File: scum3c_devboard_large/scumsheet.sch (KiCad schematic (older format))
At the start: 15 parts, among them U8 scum3

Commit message: ready for merge
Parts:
- removed C13, C14, C15, C16, C17, C18, C19, C20, C21, C22, C24: NP, Capacitor_SMD:C_0402_1005Metric, symbol Device:C
- removed R12, R13, R14: NP, Resistor_SMD:R_0402_1005Metric, symbol Device:R_US
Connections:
- net labels removed: +VDD25, +VDDAO, AUX_LDO_OUTPUT, GP4, GP5, GP6, GP7, VDDD_DISABLE, VDD_AO_DISABLE
- wire segments 24 -> 0
- no-connect marks 44 -> 52

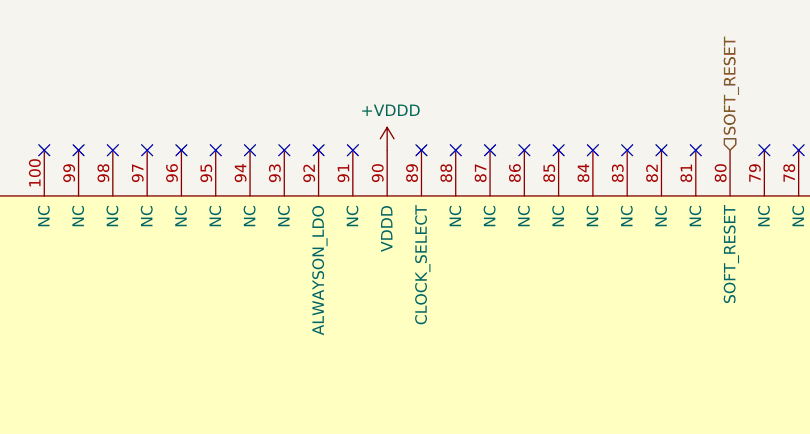
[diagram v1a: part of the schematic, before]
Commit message: replaced level shifters and other changes
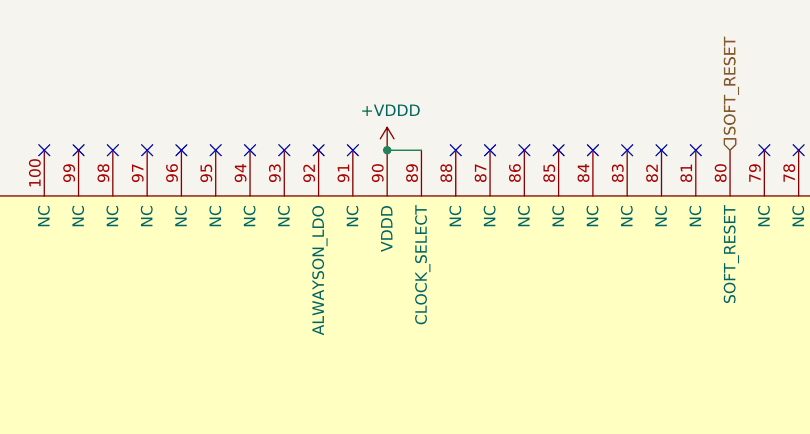
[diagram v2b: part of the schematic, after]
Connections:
- net +VDDD: now also U8.89 (CLOCK_SELECT)
- no-connect marks 52 -> 51
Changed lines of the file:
@@
 NoConn ~ 2250 3800
 NoConn ~ 2250 4550
-NoConn ~ 2250 4700
 NoConn ~ 2250 4850
 NoConn ~ 2250 5000
@@
 NoConn ~ 2250 5450
 NoConn ~ 2250 5600
-NoConn ~ 8000 1950
 NoConn ~ 8000 2100
 NoConn ~ 8000 2250
@@
 NoConn ~ 8000 2550
 NoConn ~ 8000 2700
-NoConn ~ 5000 1150
 NoConn ~ 2250 3350
 NoConn ~ 2250 5150
-NoConn ~ 8000 2400
 NoConn ~ 2250 3650
 NoConn ~ 4550 1150
+NoConn ~ 8000 2400
+Wire Wire Line
+	5000 1150 4850 1150
+Connection ~ 4850 1150
+NoConn ~ 2250 4700
+NoConn ~ 8000 1950
 $EndSCHEMATC

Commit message: Suggested changes
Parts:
- added J14, J15: Conn_01x01_Male, Connector_PinHeader_2.54mm:PinHeader_1x01_P2.54mm_Vertical, symbol Connector:Conn_01x01_Male
- U8: symbol draft1library:scum3 -> SCUM:scum3
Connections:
- net at U8.53 (SENSOR_LDO_OUTPUT): now also J15.1 (Pin_1)
- net at U8.54 (SENSOR_EXT_IN): now also J14.1 (Pin_1)
- no-connect marks 51 -> 49
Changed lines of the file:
@@
 EESchema Schematic File Version 4
 LIBS:scum3c-devboard-cache
-EELAYER 26 0
+EELAYER 30 0
 EELAYER END
 $Descr A4 11693 8268
 encoding utf-8
-Sheet 2 4
+Sheet 4 4
 Title ""
 Date ""
@@
 $EndDescr
 $Comp
-L draft1library:scum3 U8
+L SCUM:scum3 U8
 U 1 1 5F3B2246
 P 5200 3450
@@
 NoConn ~ 8000 5550
 NoConn ~ 8000 5400
-NoConn ~ 8000 5250
-NoConn ~ 8000 5100
 NoConn ~ 6950 1150
 NoConn ~ 6800 1150
@@
 $EndComp
 $Comp
-L draft1library:+VBAT #PWR0170
+L SCUM:+VBAT #PWR0170
 U 1 1 5F3D3274
 P 2250 2450
@@
 $EndComp
 $Comp
-L draft1library:+VBAT #PWR0176
+L SCUM:+VBAT #PWR0176
 U 1 1 5F3DA21E
 P 2250 4400
@@
 $EndComp
 $Comp
-L draft1library:+VBAT #PWR0193
+L SCUM:+VBAT #PWR0193
 U 1 1 5F40149D
 P 3100 6050
@@
 GPIO15
 $Comp
-L draft1library:+VDDIO #PWR0194
+L SCUM:+VDDIO #PWR0194
 U 1 1 5F404D67
 P 4900 6050
@@
 HARD_RESET
 $Comp
-L draft1library:+VBAT #PWR0195
+L SCUM:+VBAT #PWR0195
 U 1 1 5F406DAE
 P 8000 4350
@@
 ASC_PHI2
 $Comp
-L draft1library:+VBAT #PWR0196
+L SCUM:+VBAT #PWR0196
 U 1 1 5F407E52
 P 8000 3900
@@
 ASC_EXT_OVERRIDE
 $Comp
-L draft1library:+VDDD #PWR0207
+L SCUM:+VDDD #PWR0207
 U 1 1 5F3A7150
 P 4850 1150
@@
 Wire Wire Line
 	5000 1150 4850 1150
-Connection ~ 4850 1150
 NoConn ~ 2250 4700
 NoConn ~ 8000 1950
+$Comp
+L Connector:Conn_01x01_Male J14
+U 1 1 607AD522
+P 8200 5100
+F 0 "J14" H 8172 5032 50  0000 R CNN
+F 1 "Conn_01x01_Male" H 8172 5123 50  0000 R CNN
+F 2 "Connector_PinHeader_2.54mm:PinHeader_1x01_P2.54mm_Vertical" H 8200 5100 50  0001 C CNN
+F 3 "~" H 8200 5100 50  0001 C CNN
+	1    8200 5100
+	-1   0    0    1
+$EndComp
+$Comp
+L Connector:Conn_01x01_Male J15
+U 1 1 607AEA7E
+P 8200 5250
+F 0 "J15" H 8172 5182 50  0000 R CNN
+F 1 "Conn_01x01_Male" H 8172 5273 50  0000 R CNN
+F 2 "Connector_PinHeader_2.54mm:PinHeader_1x01_P2.54mm_Vertical" H 8200 5250 50  0001 C CNN
+F 3 "~" H 8200 5250 50  0001 C CNN
+	1    8200 5250
+	-1   0    0    1
+$EndComp
 $EndSCHEMATC

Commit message: switching computers
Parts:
- removed J14, J15: Conn_01x01_Male, Connector_PinHeader_2.54mm:PinHeader_1x01_P2.54mm_Vertical, symbol Connector:Conn_01x01_Male
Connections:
- net ADC_LDO_OUT: now reaches U8.53 (SENSOR_LDO_OUTPUT)
- net ADC_IN: now reaches U8.54 (SENSOR_EXT_IN)
- net GPO_ZERO: now reaches U8.57 (GPO_ZERO)
- net +VBAT renamed +VBATSCuM
- net +VDDIO renamed +VDDIOSCuM
- net SOFT_RESET: no longer names the net of U8.80 (SOFT_RESET)
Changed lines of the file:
@@
 NoConn ~ 8000 2100
 NoConn ~ 8000 2250
-NoConn ~ 8000 4650
 NoConn ~ 8000 5550
 NoConn ~ 8000 5400
@@
 $EndComp
 $Comp
-L SCUM:+VBAT #PWR0170
-U 1 1 5F3D3274
-P 2250 2450
-AR Path="/5F3B1D81/5F3D3274" Ref="#PWR0170"  Part="1"
-AR Path="/5F41418C/5F3D3274" Ref="#PWR?"  Part="1"
-AR Path="/5F414989/5F3D3274" Ref="#PWR?"  Part="1"
-F 0 "#PWR0170" H 2250 2300 50  0001 C CNN
-F 1 "+VBAT" V 2265 2578 50  0000 L CNN
-F 2 "" H 2250 2450 50  0001 C CNN
-F 3 "" H 2250 2450 50  0001 C CNN
-	1    2250 2450
-	0    -1   -1   0
-$EndComp
-$Comp
 L power:GND #PWR0171
 U 1 1 5F3D443B
@@
 	1    2250 4250
 	0    1    1    0
-$EndComp
-$Comp
-L SCUM:+VBAT #PWR0176
-U 1 1 5F3DA21E
-P 2250 4400
-AR Path="/5F3B1D81/5F3DA21E" Ref="#PWR0176"  Part="1"
-AR Path="/5F41418C/5F3DA21E" Ref="#PWR?"  Part="1"
-AR Path="/5F414989/5F3DA21E" Ref="#PWR?"  Part="1"
-F 0 "#PWR0176" H 2250 4250 50  0001 C CNN
-F 1 "+VBAT" V 2265 4528 50  0000 L CNN
-F 2 "" H 2250 4400 50  0001 C CNN
-F 3 "" H 2250 4400 50  0001 C CNN
-	1    2250 4400
-	0    -1   -1   0
 $EndComp
 $Comp
@@
 	1    8000 2850
 	0    -1   -1   0
-$EndComp
-$Comp
-L SCUM:+VBAT #PWR0193
-U 1 1 5F40149D
-P 3100 6050
-AR Path="/5F3B1D81/5F40149D" Ref="#PWR0193"  Part="1"
-AR Path="/5F41418C/5F40149D" Ref="#PWR?"  Part="1"
-AR Path="/5F414989/5F40149D" Ref="#PWR?"  Part="1"
-F 0 "#PWR0193" H 3100 5900 50  0001 C CNN
-F 1 "+VBAT" H 3115 6223 50  0000 C CNN
-F 2 "" H 3100 6050 50  0001 C CNN
-F 3 "" H 3100 6050 50  0001 C CNN
-	1    3100 6050
-	-1   0    0    1
 $EndComp
 Text HLabel 3850 6050 3    50   BiDi ~ 0
@@
 Text HLabel 6100 6050 3    50   BiDi ~ 0
 GPIO15
-$Comp
-L SCUM:+VDDIO #PWR0194
-U 1 1 5F404D67
-P 4900 6050
-AR Path="/5F3B1D81/5F404D67" Ref="#PWR0194"  Part="1"
-AR Path="/5F41418C/5F404D67" Ref="#PWR?"  Part="1"
-AR Path="/5F414989/5F404D67" Ref="#PWR?"  Part="1"
-F 0 "#PWR0194" H 4900 5900 50  0001 C CNN
-F 1 "+VDDIO" H 4915 6223 50  0000 C CNN
-F 2 "" H 4900 6050 50  0001 C CNN
-F 3 "" H 4900 6050 50  0001 C CNN
-	1    4900 6050
-	-1   0    0    1
-$EndComp
 Text HLabel 6450 6050 3    50   Output ~ 0
 RsTx
@@
 Text HLabel 8000 4200 2    50   BiDi ~ 0
 HARD_RESET
-$Comp
-L SCUM:+VBAT #PWR0195
-U 1 1 5F406DAE
-P 8000 4350
-AR Path="/5F3B1D81/5F406DAE" Ref="#PWR0195"  Part="1"
-AR Path="/5F41418C/5F406DAE" Ref="#PWR?"  Part="1"
-AR Path="/5F414989/5F406DAE" Ref="#PWR?"  Part="1"
-F 0 "#PWR0195" H 8000 4200 50  0001 C CNN
-F 1 "+VBAT" V 8015 4478 50  0000 L CNN
-F 2 "" H 8000 4350 50  0001 C CNN
-F 3 "" H 8000 4350 50  0001 C CNN
-	1    8000 4350
-	0    1    1    0
-$EndComp
 Text HLabel 8000 3750 2    50   BiDi ~ 0
 ASC_PHI2
-$Comp
-L SCUM:+VBAT #PWR0196
-U 1 1 5F407E52
-P 8000 3900
-AR Path="/5F3B1D81/5F407E52" Ref="#PWR0196"  Part="1"
-AR Path="/5F41418C/5F407E52" Ref="#PWR?"  Part="1"
-AR Path="/5F414989/5F407E52" Ref="#PWR?"  Part="1"
-F 0 "#PWR0196" H 8000 3750 50  0001 C CNN
-F 1 "+VBAT" V 8015 4028 50  0000 L CNN
-F 2 "" H 8000 3900 50  0001 C CNN
-F 3 "" H 8000 3900 50  0001 C CNN
-	1    8000 3900
-	0    1    1    0
-$EndComp
 Text HLabel 8000 3600 2    50   BiDi ~ 0
 ASC_PHI1
@@
 Text HLabel 2250 4100 0    50   BiDi ~ 0
 RF_IN
-Text HLabel 6350 1150 1    50   Input ~ 0
-SOFT_RESET
 Text HLabel 8000 4050 2    50   Input ~ 0
 BOOT_SOURCE_SEL
@@
 NoConn ~ 2250 4700
 NoConn ~ 8000 1950
-$Comp
-L Connector:Conn_01x01_Male J14
-U 1 1 607AD522
-P 8200 5100
-F 0 "J14" H 8172 5032 50  0000 R CNN
-F 1 "Conn_01x01_Male" H 8172 5123 50  0000 R CNN
-F 2 "Connector_PinHeader_2.54mm:PinHeader_1x01_P2.54mm_Vertical" H 8200 5100 50  0001 C CNN
-F 3 "~" H 8200 5100 50  0001 C CNN
-	1    8200 5100
+Text HLabel 8000 5100 2    50   Input ~ 0
+ADC_IN
+Text HLabel 8000 5250 2    50   Input ~ 0
+ADC_LDO_OUT
+$Comp
+L SCUM:+VBATSCuM #PWR0238
+U 1 1 6096A367
+P 8000 3900
+F 0 "#PWR0238" H 8000 3750 50  0001 C CNN
+F 1 "+VBATSCuM" V 8015 4028 50  0000 L CNN
+F 2 "" H 8000 3900 50  0001 C CNN
+F 3 "" H 8000 3900 50  0001 C CNN
+	1    8000 3900
+	0    1    1    0
+$EndComp
+$Comp
+L SCUM:+VBATSCuM #PWR0239
+U 1 1 6096ADFE
+P 8000 4350
+F 0 "#PWR0239" H 8000 4200 50  0001 C CNN
+F 1 "+VBATSCuM" V 8015 4478 50  0000 L CNN
+F 2 "" H 8000 4350 50  0001 C CNN
+F 3 "" H 8000 4350 50  0001 C CNN
+	1    8000 4350
+	0    1    1    0
+$EndComp
+$Comp
+L SCUM:+VBATSCuM #PWR0240
+U 1 1 6096BA20
+P 3100 6050
+F 0 "#PWR0240" H 3100 5900 50  0001 C CNN
+F 1 "+VBATSCuM" V 3100 6400 50  0000 C CNN
+F 2 "" H 3100 6050 50  0001 C CNN
+F 3 "" H 3100 6050 50  0001 C CNN
+	1    3100 6050
 	-1   0    0    1
 $EndComp
 $Comp
-L Connector:Conn_01x01_Male J15
-U 1 1 607AEA7E
-P 8200 5250
-F 0 "J15" H 8172 5182 50  0000 R CNN
-F 1 "Conn_01x01_Male" H 8172 5273 50  0000 R CNN
-F 2 "Connector_PinHeader_2.54mm:PinHeader_1x01_P2.54mm_Vertical" H 8200 5250 50  0001 C CNN
-F 3 "~" H 8200 5250 50  0001 C CNN
-	1    8200 5250
+L SCUM:+VBATSCuM #PWR0241
+U 1 1 6096CDC5
+P 2250 4400
+F 0 "#PWR0241" H 2250 4250 50  0001 C CNN
+F 1 "+VBATSCuM" V 2265 4528 50  0000 L CNN
+F 2 "" H 2250 4400 50  0001 C CNN
+F 3 "" H 2250 4400 50  0001 C CNN
+	1    2250 4400
+	0    -1   -1   0
+$EndComp
+$Comp
+L SCUM:+VDDIOSCuM #PWR0242
+U 1 1 6096DAC9
+P 4900 6050
+F 0 "#PWR0242" H 4900 5900 50  0001 C CNN
+F 1 "+VDDIOSCuM" V 4900 6400 50  0000 C CNN
+F 2 "" H 4900 6050 50  0001 C CNN
+F 3 "" H 4900 6050 50  0001 C CNN
+	1    4900 6050
 	-1   0    0    1
 $EndComp
+$Comp
+L SCUM:+VBATSCuM #PWR0243
+U 1 1 6096E5D5
+P 2250 2450
+F 0 "#PWR0243" H 2250 2300 50  0001 C CNN
+F 1 "+VBATSCuM" V 2265 2578 50  0000 L CNN
+F 2 "" H 2250 2450 50  0001 C CNN
+F 3 "" H 2250 2450 50  0001 C CNN
+	1    2250 2450
+	0    -1   -1   0
+$EndComp
+NoConn ~ 6350 1150
+Text HLabel 8000 4650 2    50   Input ~ 0
+GPO_ZERO
 $EndSCHEMATC
